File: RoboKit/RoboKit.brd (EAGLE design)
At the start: 134 x 82 mm, 32 parts, among them CON1 XT30UPB-M, CON2 XT30UPB-M, P1 B6B-PH-K, P2 B6B-PH-K, U1 SSM6J808R, X3 JST-XH-02-PIN-LONG-PAD, X4 JST-XH-02-PIN-LONG-PAD, X5 JST-XH-04-PIN-LONG-PAD, X6 JST-XH-04-PIN-LONG-PAD, X7 JST-XH-10-PIN-LONG-PAD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

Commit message: テスト8
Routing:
- net IO15: track 30.2 -> 30.7 mm
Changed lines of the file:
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@@
 <wire x1="87.3125" y1="76.2" x2="79.0575" y2="76.2" width="1" layer="16"/>
 <via x="87.3125" y="76.2" extent="1-16" drill="0.35"/>
-<wire x1="87.3125" y1="76.2" x2="94.615" y2="76.2" width="1" layer="1"/>
-<wire x1="95.9612" y1="74.8538" x2="95.9612" y2="73.3044" width="1" layer="1"/>
-<wire x1="94.615" y1="76.2" x2="95.9612" y2="74.8538" width="1" layer="1"/>
+<wire x1="87.3125" y1="76.2" x2="95.5675" y2="76.2" width="1" layer="1"/>
+<wire x1="95.9612" y1="75.8063" x2="95.9612" y2="73.3044" width="1" layer="1"/>
+<wire x1="95.5675" y1="76.2" x2="95.9612" y2="75.8063" width="1" layer="1"/>
 </signal>
 <signal name="VBUS" class="2">

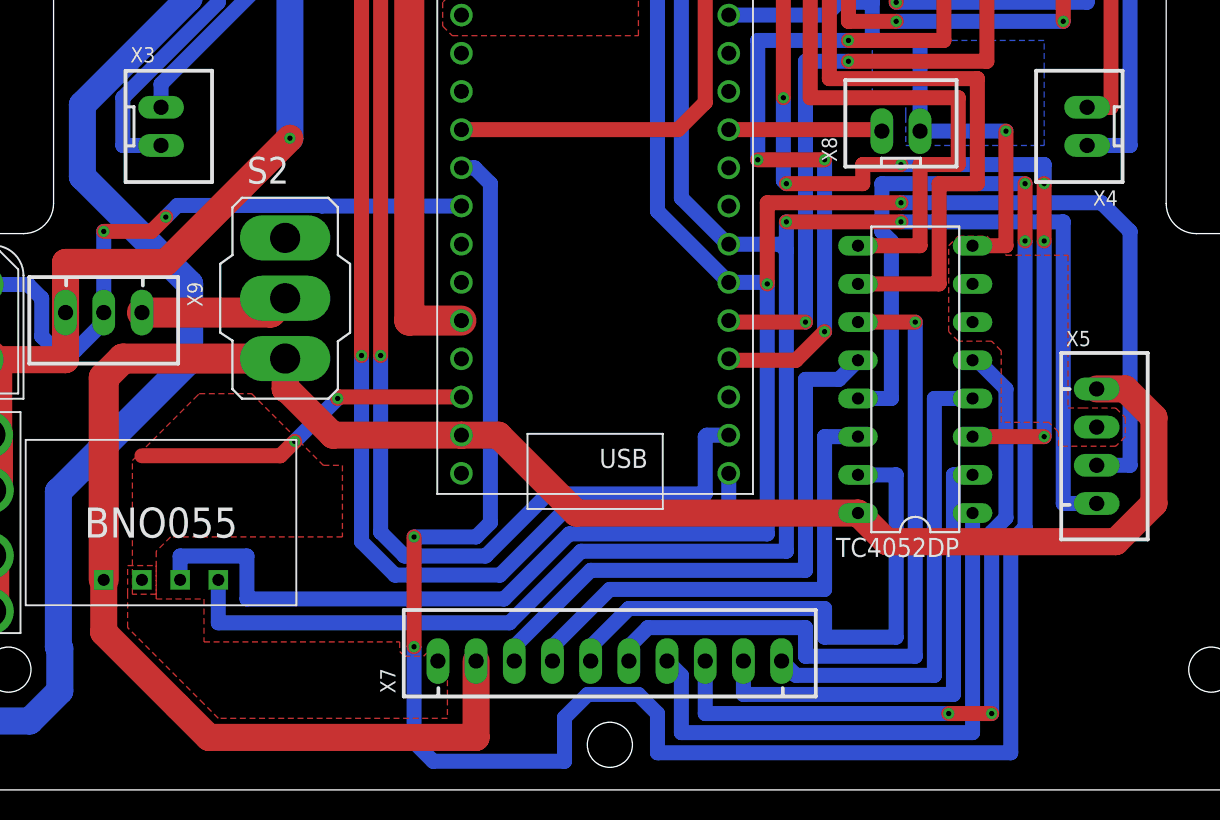
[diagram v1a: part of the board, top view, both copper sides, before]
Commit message: 信号線の太さを変更
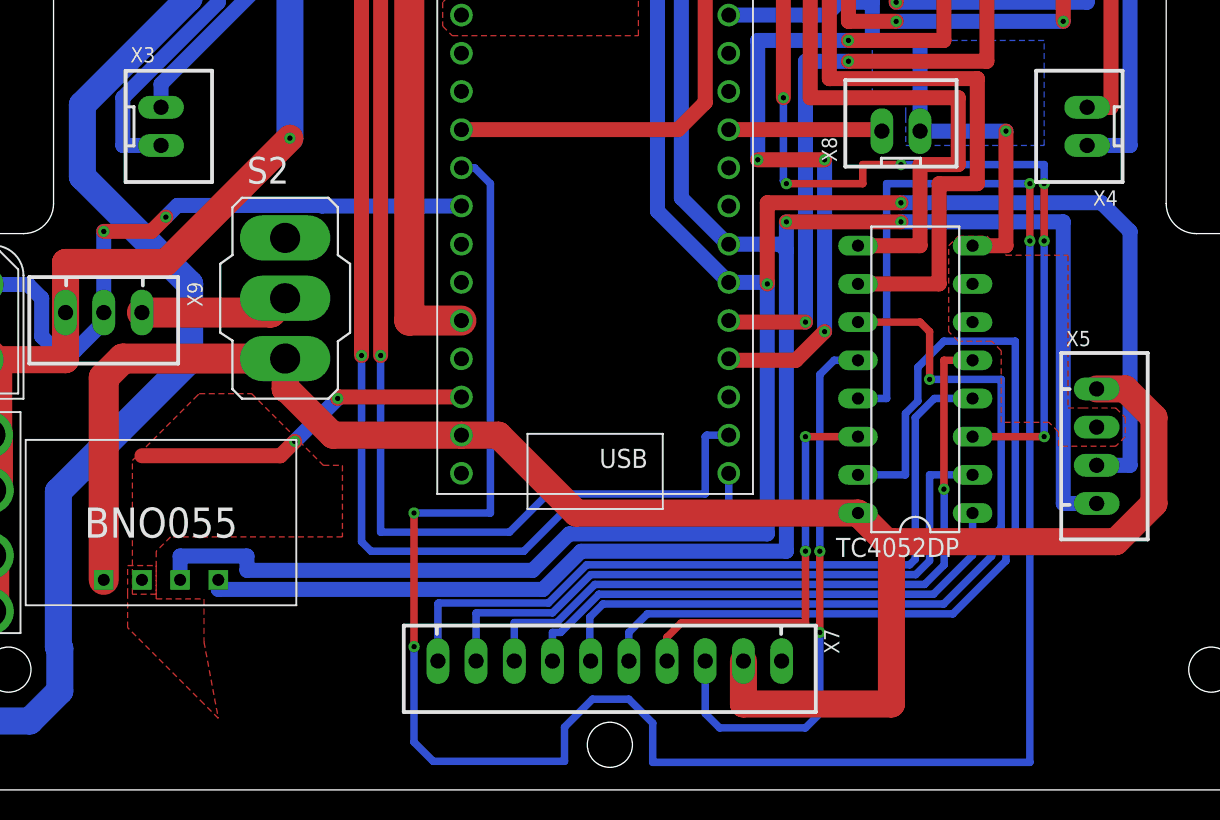
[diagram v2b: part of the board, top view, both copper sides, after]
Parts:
- turned X7 to 180 degrees
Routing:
- net 2X: track 37.6 -> 61.7 mm
- net 3Y: track 31.5 -> 50.5 mm
- net VSYS: track 137.8 -> 125.0 mm
- net 2Y: track 32.1 -> 43.4 mm
- net 3X: track 48.5 -> 56.3 mm
- net 1X: track 33.0 -> 27.1 mm, vias 0 -> 2
- net 0Y: track 39.1 -> 34.8 mm
- net SCL: track 150.6 -> 147.4 mm
- net SDA: track 158.9 -> 156.2 mm
- net 0X: track 39.1 -> 37.4 mm, vias 0 -> 2
- net IO0: track 81.3 -> 80.0 mm
- net IO1: track 77.0 -> 75.7 mm
- net X-COM: track 155.5 -> 156.6 mm
- net 1Y: track 47.5 -> 48.3 mm, vias 2 -> 1

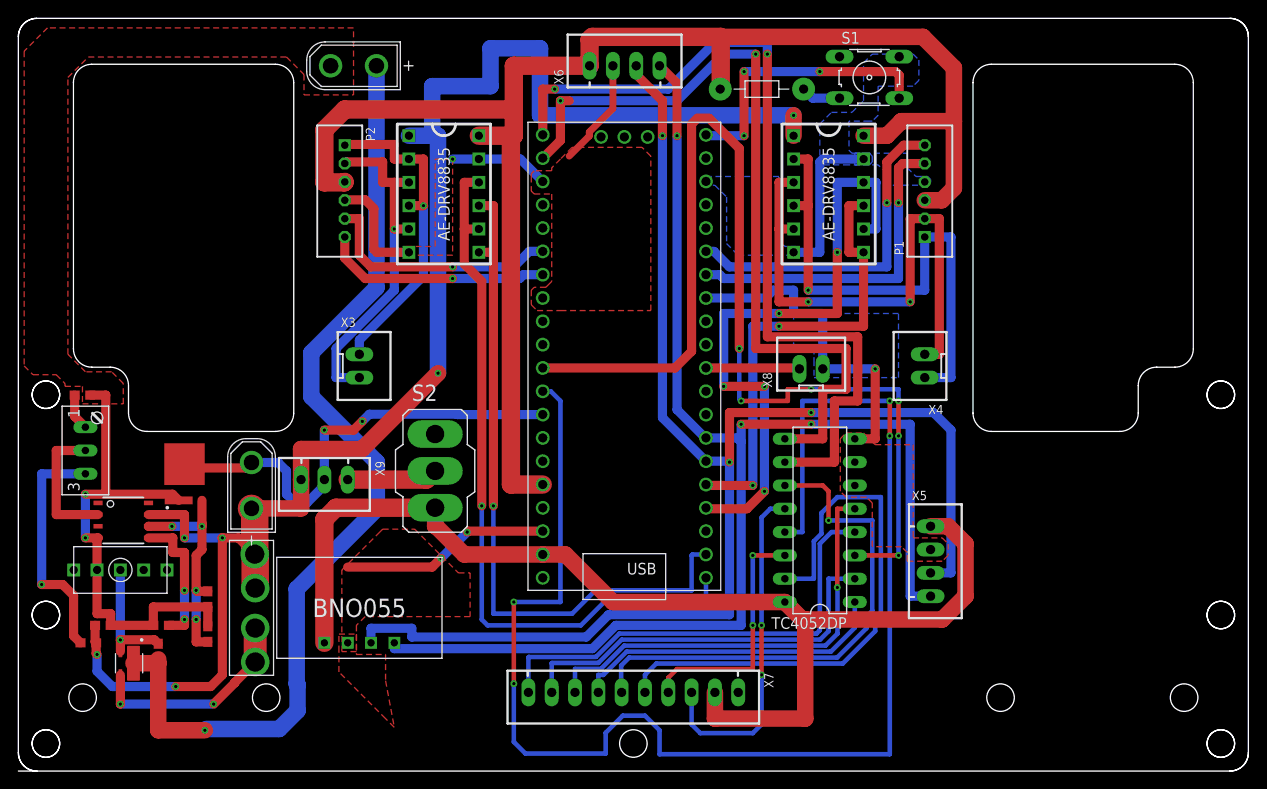
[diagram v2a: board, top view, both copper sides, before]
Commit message: 信号線の太さを変更
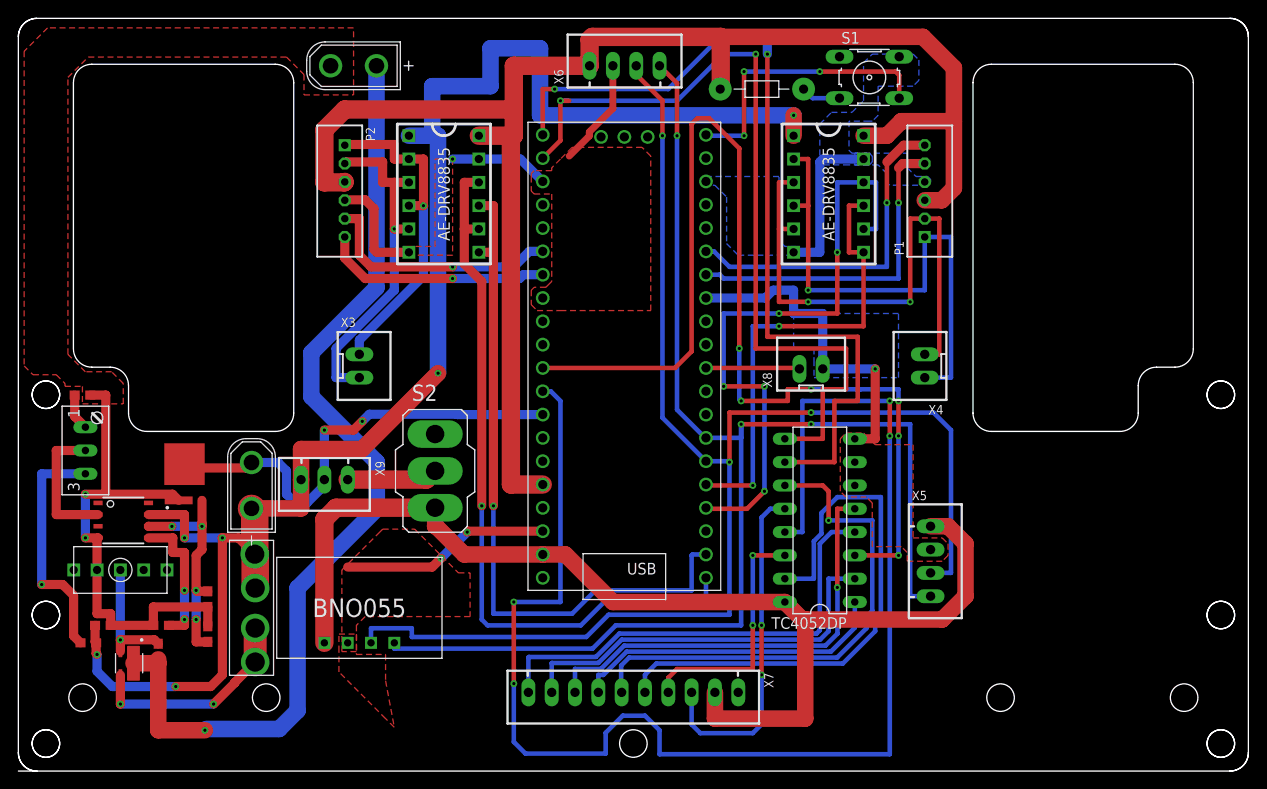
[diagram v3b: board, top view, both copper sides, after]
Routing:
- net SCL: track 147.4 -> 148.7 mm

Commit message: ポリゴンの範囲を拡大
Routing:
- net GND: track 163.1 -> 190.0 mm, vias 6 -> 8
- net IO2: track 68.3 -> 64.8 mm
- net SCL: track 148.7 -> 145.2 mm
- net SDA: track 156.3 -> 154.2 mm
- net IO1: track 75.7 -> 77.5 mm
- net Y-COM: track 117.4 -> 115.8 mm
- net MOTOR_A_R: track 57.0 -> 55.5 mm
- net IO0: track 80.0 -> 81.0 mm
- net HALL_B_R: track 36.7 -> 37.4 mm
- net MOTOR_B_R: track 59.1 -> 58.5 mm
- net A: track 95.1 -> 94.4 mm
- net IO3: track 50.9 -> 50.3 mm
- net VIN: vias 1 -> 4
- net VOUT: vias 6 -> 7
- added copper zone on layer 1, net 3V3
- added copper zone on layer 16, net VIN
- added copper zone on layer 1, net VOUT
- added copper zone on layer 16, net VOUT
- added copper zone on layer 1, net VSYS

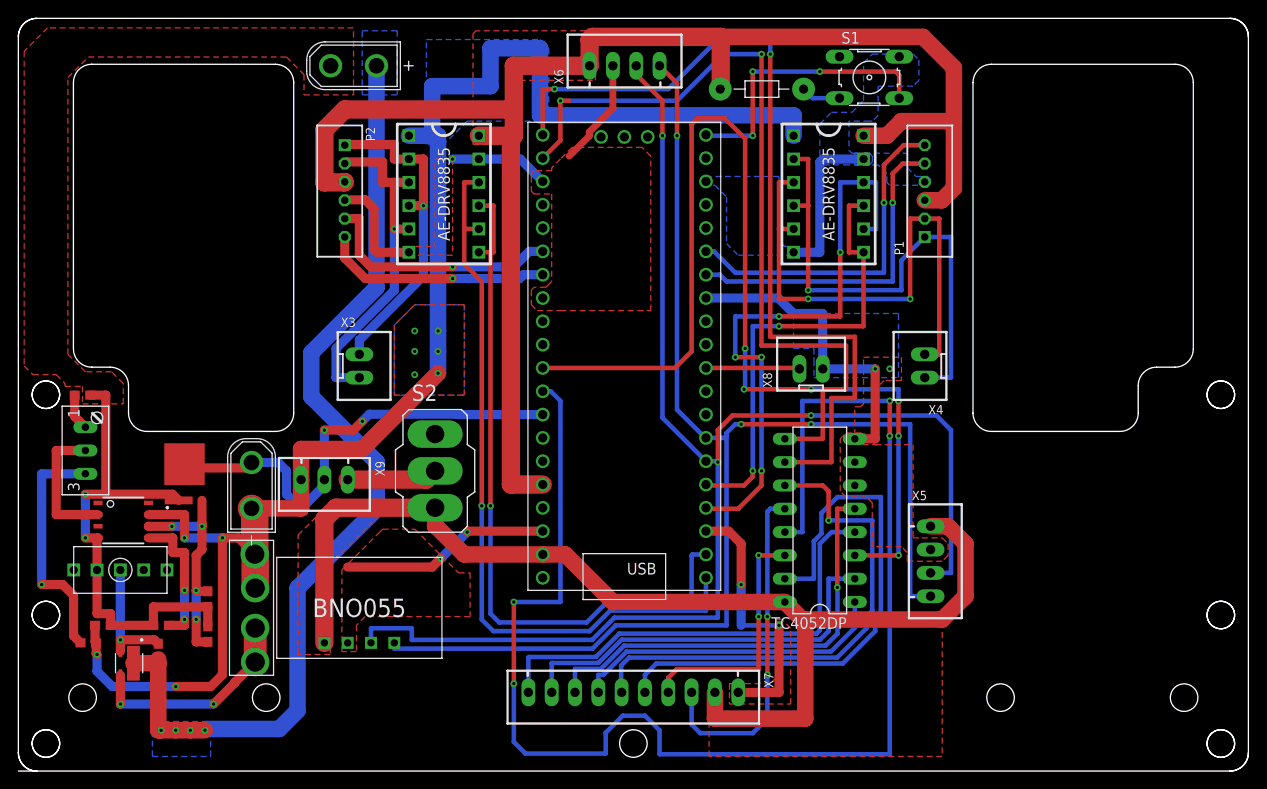
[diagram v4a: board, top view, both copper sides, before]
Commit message: ポリゴンの面積を拡大
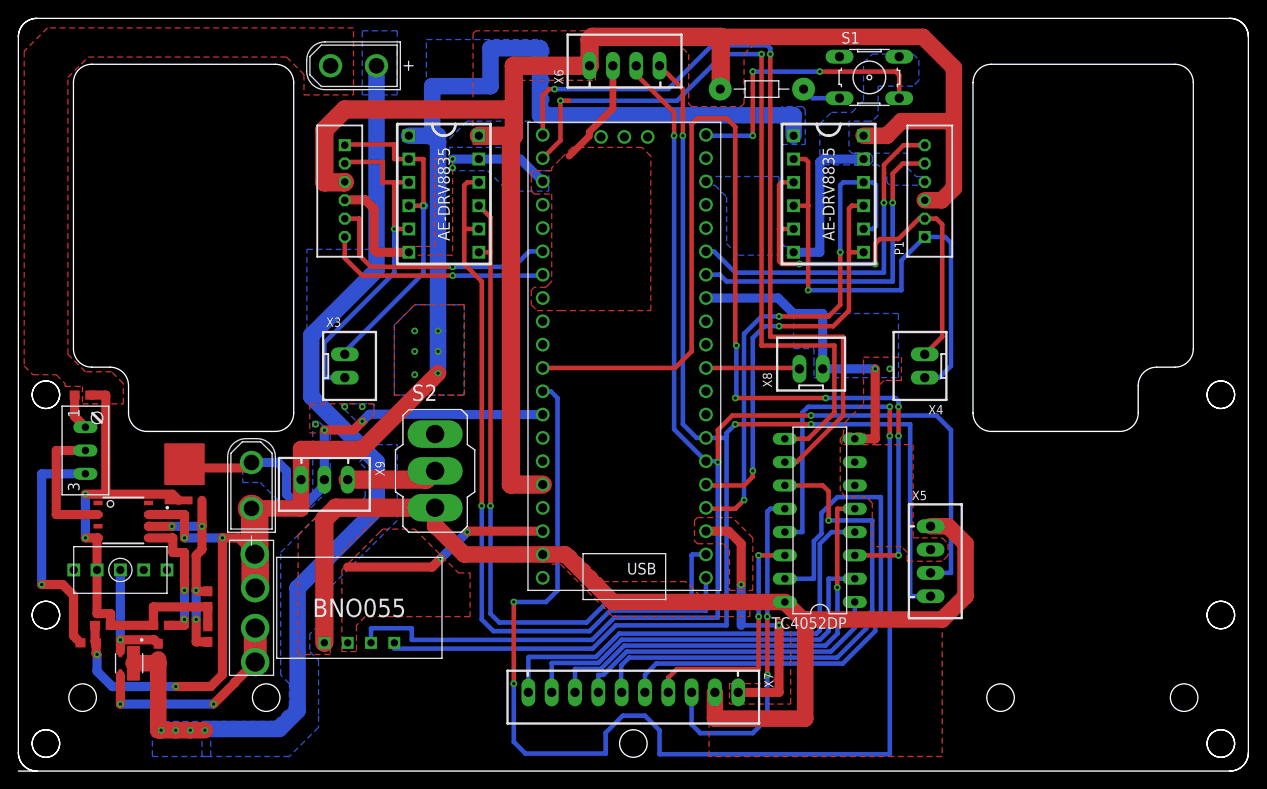
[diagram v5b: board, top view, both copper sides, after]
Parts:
- moved X3 1.59 mm to (35.6, 44.1)
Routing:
- net MOTOR_B_R: track 58.5 -> 48.0 mm
- net IO2: track 64.8 -> 57.6 mm, vias 5 -> 3
- net A: track 94.4 -> 87.9 mm
- net B: track 89.8 -> 85.6 mm
- net IO3: track 50.3 -> 46.8 mm
- net X-COM: track 156.6 -> 153.8 mm
- net IO1: track 77.5 -> 76.2 mm
- net MOTOR_A_R: track 55.5 -> 54.2 mm
- net MOTOR_A_L: track 36.0 -> 36.7 mm
- net SCL: track 145.2 -> 145.8 mm
